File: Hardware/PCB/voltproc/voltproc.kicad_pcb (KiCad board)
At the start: 2 copper layers, 171 x 174 mm, 85 parts, among them J1 Synth_power_2x5, J10 Jack, J11 Jack, J12 Jack, J13 Jack, J14 Jack, J15 Jack, J16 Jack, J17 Jack, J18 Jack, J19 Jack, J2 3_pin_Molex_header, J3 3_pin_Molex_header, J4 Conn_01x13, J7 Conn_01x13, J8 Jack, J9 Jack, SW1 SW_DPDT_x2, SW2 SW_DPDT_x2, U1 TL074, U2 TL074, U3 TL072

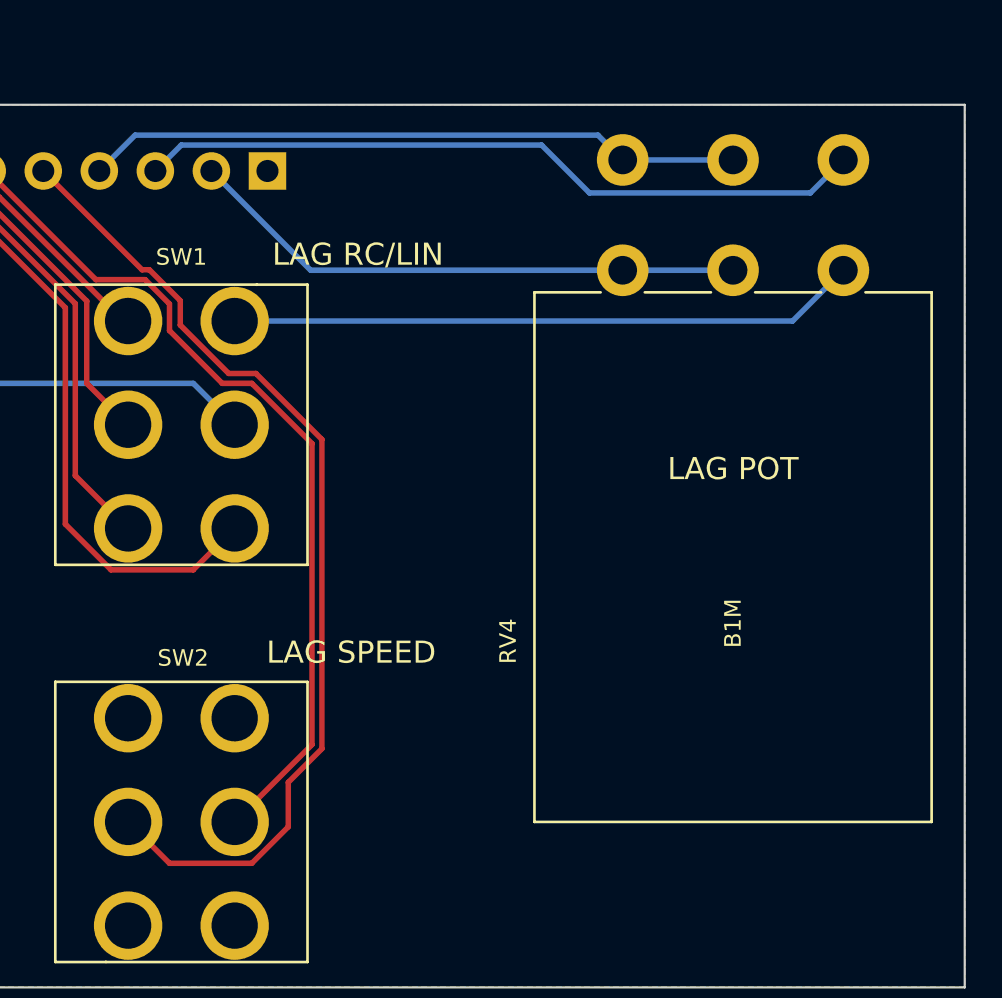
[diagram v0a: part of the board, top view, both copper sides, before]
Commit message: Fix dual pot footprint
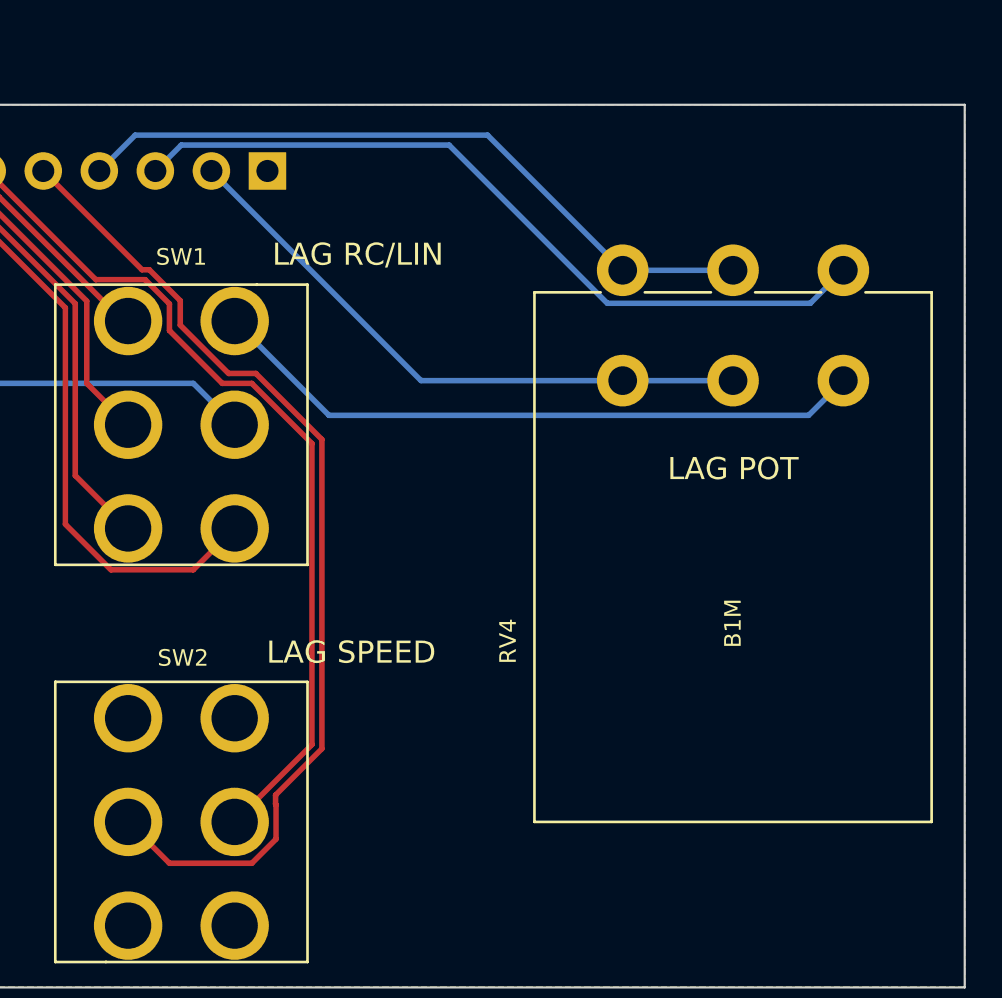
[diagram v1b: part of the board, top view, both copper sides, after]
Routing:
- net /Panel components/LAG_LIN_CCW: track 33.2 -> 35.3 mm
- net /Panel components/LAG_RC_WIP: track 25.5 -> 27.6 mm
- net /Panel components/LAG_LIN_WIP: track 29.9 -> 31.9 mm
- net /Panel components/RC_IN: track 28.5 -> 30.0 mm
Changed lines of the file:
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@@
       (effects (font (size 1 1) (thickness 0.15)))
     )
-    (fp_line (start 9 9) (end -15 9) (layer "F.SilkS") (width 0.12))
+    (fp_line (start -15 4) (end -15 1) (layer "F.SilkS") (width 0.12))
+    (fp_line (start -15 -1) (end -15 -4) (layer "F.SilkS") (width 0.12))
     (fp_line (start -15 -6) (end -15 -9) (layer "F.SilkS") (width 0.12))
+    (fp_line (start 9 9) (end -15 9) (layer "F.SilkS") (width 0.12))
     (fp_line (start -15 9) (end -15 6) (layer "F.SilkS") (width 0.12))
-    (fp_line (start -15 -1) (end -15 -4) (layer "F.SilkS") (width 0.12))
     (fp_line (start -15 -9) (end 9 -9) (layer "F.SilkS") (width 0.12))
-    (fp_line (start -15 4) (end -15 1) (layer "F.SilkS") (width 0.12))
     (fp_line (start 9 -9) (end 9 9) (layer "F.SilkS") (width 0.12))
-    (fp_line (start -22.5 9.5) (end -22.5 -9.5) (layer "F.CrtYd") (width 0.12))
-    (fp_line (start -22.5 -9.5) (end 9.5 -9.5) (layer "F.CrtYd") (width 0.12))
+    (fp_line (start -17.5 9.5) (end -17.5 -9.5) (layer "F.CrtYd") (width 0.12))
     (fp_line (start 9.5 -9.5) (end 9.5 9.5) (layer "F.CrtYd") (width 0.12))
-    (fp_line (start 9.5 9.5) (end -22.5 9.5) (layer "F.CrtYd") (width 0.12))
-    (fp_circle (center 0 0) (end 8.45 0) (layer "F.Fab") (width 0.12) (fill none))
+    (fp_line (start -17.5 -9.5) (end 9.5 -9.5) (layer "F.CrtYd") (width 0.12))
+    (fp_line (start 9.5 9.5) (end -17.5 9.5) (layer "F.CrtYd") (width 0.12))
     (fp_circle (center 0 0) (end 3 0) (layer "F.Fab") (width 0.1) (fill none))
-    (pad "1" thru_hole circle (at -21 -5 270) (size 2.34 2.34) (drill 1.3) (layers *.Cu *.Mask)
+    (fp_circle (center 0 0) (end 8.45 0) (layer "F.Fab") (width 0.12) (fill none))
+    (pad "1" thru_hole circle (at -16 -5 270) (size 2.34 2.34) (drill 1.3) (layers *.Cu *.Mask)
       (net 61 "/Panel components/LAG_LIN_CCW") (pinfunction "1") (pintype "passive"))
-    (pad "2" thru_hole circle (at -21 0 270) (size 2.34 2.34) (drill 1.3) (layers *.Cu *.Mask)
+    (pad "2" thru_hole circle (at -16 0 270) (size 2.34 2.34) (drill 1.3) (layers *.Cu *.Mask)
       (net 62 "/Panel components/LAG_LIN_WIP") (pinfunction "2") (pintype "passive"))
-    (pad "3" thru_hole circle (at -21 5 270) (size 2.34 2.34) (drill 1.3) (layers *.Cu *.Mask)
+    (pad "3" thru_hole circle (at -16 5 270) (size 2.34 2.34) (drill 1.3) (layers *.Cu *.Mask)
       (net 62 "/Panel components/LAG_LIN_WIP") (pinfunction "3") (pintype "passive"))
-    (pad "4" thru_hole circle (at -16 -5 270) (size 2.34 2.34) (drill 1.3) (layers *.Cu *.Mask)
+    (pad "4" thru_hole circle (at -11 -5 270) (size 2.34 2.34) (drill 1.3) (layers *.Cu *.Mask)
       (net 29 "/Panel components/RC_IN") (pinfunction "4") (pintype "passive"))
-    (pad "5" thru_hole circle (at -16 0 270) (size 2.34 2.34) (drill 1.3) (layers *.Cu *.Mask)
+    (pad "5" thru_hole circle (at -11 0 270) (size 2.34 2.34) (drill 1.3) (layers *.Cu *.Mask)
       (net 60 "/Panel components/LAG_RC_WIP") (pinfunction "5") (pintype "passive"))
-    (pad "6" thru_hole circle (at -16 5 270) (size 2.34 2.34) (drill 1.3) (layers *.Cu *.Mask)
+    (pad "6" thru_hole circle (at -11 5 270) (size 2.34 2.34) (drill 1.3) (layers *.Cu *.Mask)
       (net 60 "/Panel components/LAG_RC_WIP") (pinfunction "6") (pintype "passive"))
     (model "${KICAD_AOKICAD}/ao_tht_3d/Potentiometer_Piher_PC-16_Single_Vertical.wrl"
@@
   (segment (start 199.459511 105.733511) (end 201.851489 108.125489) (width 0.25) (layer "F.Cu") (net 23))
   (segment (start 196.125489 103.425489) (end 198.361449 103.425489) (width 0.25) (layer "F.Cu") (net 23))
-  (segment (start 204.843511 126.207193) (end 204.843511 128.222449) (width 0.25) (layer "F.Cu") (net 24))
+  (segment (start 199.949 105.48496) (end 202.140018 107.675978) (width 0.25) (layer "F.Cu") (net 24))
+  (segment (start 204.29 127.223349) (end 204.29 128.776651) (width 0.25) (layer "F.Cu") (net 24))
   (segment (start 206.367511 110.665847) (end 206.367511 124.683193) (width 0.25) (layer "F.Cu") (net 24))
-  (segment (start 203.377643 107.675979) (end 206.367511 110.665847) (width 0.25) (layer "F.Cu") (net 24))
-  (segment (start 202.140018 107.675978) (end 203.377643 107.675979) (width 0.25) (layer "F.Cu") (net 24))
-  (segment (start 193.74 98.5) (end 198.215978 102.975978) (width 0.25) (layer "F.Cu") (net 24))
+  (segment (start 203.19214 129.874511) (end 199.459511 129.874511) (width 0.25) (layer "F.Cu") (net 24))
   (segment (start 199.949 104.377336) (end 199.949 105.48496) (width 0.25) (layer "F.Cu") (net 24))
-  (segment (start 206.367511 124.683193) (end 204.843511 126.207193) (width 0.25) (layer "F.Cu") (net 24))
-  (segment (start 199.949 105.48496) (end 202.140018 107.675978) (width 0.25) (layer "F.Cu") (net 24))
-  (segment (start 203.191449 129.874511) (end 199.459511 129.874511) (width 0.25) (layer "F.Cu") (net 24))
+  (segment (start 204.267 127.200349) (end 204.29 127.223349) (width 0.25) (layer "F.Cu") (net 24))
   (segment (start 198.215978 102.975978) (end 198.547643 102.975979) (width 0.25) (layer "F.Cu") (net 24))
-  (segment (start 198.547643 102.975979) (end 199.949 104.377336) (width 0.25) (layer "F.Cu") (net 24))
-  (segment (start 204.843511 128.222449) (end 203.191449 129.874511) (width 0.25) (layer "F.Cu") (net 24))
   (segment (start 199.459511 129.874511) (end 197.585 128) (width 0.25) (layer "F.Cu") (net 24))
+  (segment (start 204.267 126.783704) (end 204.267 127.200349) (width 0.25) (layer "F.Cu") (net 24))
+  (segment (start 198.547643 102.975979) (end 199.949 104.377336) (width 0.25) (layer "F.Cu") (net 24))
+  (segment (start 206.367511 124.683193) (end 204.267 126.783704) (width 0.25) (layer "F.Cu") (net 24))
+  (segment (start 204.29 128.776651) (end 203.19214 129.874511) (width 0.25) (layer "F.Cu") (net 24))
+  (segment (start 203.377643 107.675979) (end 206.367511 110.665847) (width 0.25) (layer "F.Cu") (net 24))
+  (segment (start 193.74 98.5) (end 198.215978 102.975978) (width 0.25) (layer "F.Cu") (net 24))
+  (segment (start 202.140018 107.675978) (end 203.377643 107.675979) (width 0.25) (layer "F.Cu") (net 24))
   (segment (start 195.710489 108.125489) (end 197.585 110) (width 0.25) (layer "F.Cu") (net 25))
   (segment (start 195.710489 104.396081) (end 195.710489 108.125489) (width 0.25) (layer "F.Cu") (net 25))
@@
   (segment (start 181.04 98.5) (end 190.665489 108.125489) (width 0.25) (layer "B.Cu") (net 28))
   (segment (start 200.540489 108.125489) (end 202.415 110) (width 0.25) (layer "B.Cu") (net 28))
-  (segment (start 227.7 105.3) (end 230 103) (width 0.25) (layer "B.Cu") (net 29))
-  (segment (start 202.415 105.3) (end 227.7 105.3) (width 0.25) (layer "B.Cu") (net 29))
+  (segment (start 202.415 105.3) (end 206.69 109.575) (width 0.25) (layer "B.Cu") (net 29))
+  (segment (start 206.69 109.575) (end 228.425 109.575) (width 0.25) (layer "B.Cu") (net 29))
+  (segment (start 228.425 109.575) (end 230 108) (width 0.25) (layer "B.Cu") (net 29))
   (segment (start 194.742 104.699) (end 194.742 114.50796) (width 0.25) (layer "F.Cu") (net 30))
   (segment (start 184.201 99.873) (end 185.471 101.143) (width 0.25) (layer "F.Cu") (net 30))
@@
   (segment (start 91.12 108.895) (end 91.12 106.355) (width 0.25) (layer "F.Cu") (net 57))
   (segment (start 91.12 106.355) (end 96.185 106.355) (width 0.25) (layer "B.Cu") (net 57))
-  (segment (start 225 103) (end 220 103) (width 0.25) (layer "B.Cu") (net 60))
-  (segment (start 220 103) (end 205.86 103) (width 0.25) (layer "B.Cu") (net 60))
-  (segment (start 205.86 103) (end 201.36 98.5) (width 0.25) (layer "B.Cu") (net 60))
-  (segment (start 216.324489 97.325489) (end 218.493511 99.494511) (width 0.25) (layer "B.Cu") (net 61))
-  (segment (start 199.994511 97.325489) (end 216.324489 97.325489) (width 0.25) (layer "B.Cu") (net 61))
-  (segment (start 228.505489 99.494511) (end 230 98) (width 0.25) (layer "B.Cu") (net 61))
-  (segment (start 198.82 98.5) (end 199.994511 97.325489) (width 0.25) (layer "B.Cu") (net 61))
-  (segment (start 218.493511 99.494511) (end 228.505489 99.494511) (width 0.25) (layer "B.Cu") (net 61))
-  (segment (start 220 98) (end 218.875978 96.875978) (width 0.25) (layer "B.Cu") (net 62))
+  (segment (start 220 108) (end 225 108) (width 0.25) (layer "B.Cu") (net 60))
+  (segment (start 220 108) (end 210.86 108) (width 0.25) (layer "B.Cu") (net 60))
+  (segment (start 210.86 108) (end 201.36 98.5) (width 0.25) (layer "B.Cu") (net 60))
+  (segment (start 199.994521 97.325479) (end 212.133479 97.325479) (width 0.25) (layer "B.Cu") (net 61))
+  (segment (start 219.303 104.495) (end 228.505 104.495) (width 0.25) (layer "B.Cu") (net 61))
+  (segment (start 198.82 98.5) (end 199.994521 97.325479) (width 0.25) (layer "B.Cu") (net 61))
+  (segment (start 212.133479 97.325479) (end 219.303 104.495) (width 0.25) (layer "B.Cu") (net 61))
+  (segment (start 228.505 104.495) (end 230 103) (width 0.25) (layer "B.Cu") (net 61))
   (segment (start 197.904022 96.875978) (end 196.28 98.5) (width 0.25) (layer "B.Cu") (net 62))
-  (segment (start 218.875978 96.875978) (end 197.904022 96.875978) (width 0.25) (layer "B.Cu") (net 62))
-  (segment (start 225 98) (end 220 98) (width 0.25) (layer "B.Cu") (net 62))
+  (segment (start 220 103) (end 225 103) (width 0.25) (layer "B.Cu") (net 62))
+  (segment (start 213.875978 96.875978) (end 197.904022 96.875978) (width 0.25) (layer "B.Cu") (net 62))
+  (segment (start 220 103) (end 213.875978 96.875978) (width 0.25) (layer "B.Cu") (net 62))
   (segment (start 96.272614 168.6) (end 98.578614 166.294) (width 0.25) (layer "B.Cu") (net 63))
   (segment (start 105.064398 166.294) (end 119.418272 151.940126) (width 0.25) (layer "B.Cu") (net 63))

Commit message: final pre fab tweaks
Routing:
- net /Summers/OUT1: track 29.7 -> 28.9 mm
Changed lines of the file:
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@@
   (segment (start 103.81 40.31) (end 116.3916 40.31) (width 0.25) (layer "B.Cu") (net 40))
   (segment (start 116.3916 40.31) (end 120.395 44.3134) (width 0.25) (layer "B.Cu") (net 40))
-  (segment (start 123.704 53.6) (end 124.5 53.6) (width 0.25) (layer "B.Cu") (net 40))
   (segment (start 118.6 85.5) (end 118.6 82.273293) (width 0.25) (layer "F.Cu") (net 41))
   (segment (start 128.813293 72.06) (end 130.48 72.06) (width 0.25) (layer "F.Cu") (net 41))

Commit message: R7->47k; documentation and photos
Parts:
- R7: value 4.7k -> 47k

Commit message: Glare at one nonconformist jack and make it behave
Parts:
- turned J17 to -90 degrees
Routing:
- net /Summers/~{OUT1}: track 19.3 -> 9.02 mm
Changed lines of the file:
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@@
   )
   (footprint "ao_tht:Jack_6.35mm_PJ_629HAN_slots" (layer "F.Cu")
-    (at 125 85)
+    (at 125 85 -90)
     (property "Description" "1/4\" audio jack")
     (property "Sheetfile" "voltproc_summers.kicad_sch")
     (property "Sheetname" "Summers")
     (attr through_hole)
-    (fp_text reference "J17" (at 0 -9.5) (layer "F.SilkS")
+    (fp_text reference "J17" (at 0 -9.5 90) (layer "F.SilkS")
       (effects (font (size 0.75 0.75) (thickness 0.15)))
     )
-    (fp_text value "Jack" (at 0 10) (layer "F.Fab")
+    (fp_text value "Jack" (at 0 10 90) (layer "F.Fab")
       (effects (font (size 1 1) (thickness 0.15)))
     )
@@
     (fp_line (start -7.994 -7.99) (end 7.954 -7.99) (layer "F.Fab") (width 0.12))
     (fp_line (start 5.414 7.958) (end -7.994 7.958) (layer "F.Fab") (width 0.12))
-    (pad "R" thru_hole oval (at 0.5 -6.4) (size 4.500001 2.5) (drill oval 2.7 1) (layers *.Cu *.Mask))
-    (pad "RN" thru_hole oval (at 6.4 -2.5) (size 2.500001 4.500001) (drill oval 1 2.7) (layers *.Cu *.Mask))
-    (pad "S" thru_hole rect (at 4.74 4.74 45) (size 4.500001 2.500001) (drill oval 2.7 1) (layers *.Cu *.Mask)
+    (pad "R" thru_hole oval (at 0.5 -6.4 270) (size 4.500001 2.5) (drill oval 2.7 1) (layers *.Cu *.Mask))
+    (pad "RN" thru_hole oval (at 6.4 -2.5 270) (size 2.500001 4.500001) (drill oval 1 2.7) (layers *.Cu *.Mask))
+    (pad "S" thru_hole rect (at 4.74 4.74 315) (size 4.500001 2.500001) (drill oval 2.7 1) (layers *.Cu *.Mask)
       (net 2 "GND") (pintype "passive"))
-    (pad "T" thru_hole oval (at -6.4 0.5) (size 2.5 4.5) (drill oval 1 2.7) (layers *.Cu *.Mask)
+    (pad "T" thru_hole oval (at -6.4 0.5 270) (size 2.5 4.5) (drill oval 1 2.7) (layers *.Cu *.Mask)
       (net 41 "/Summers/~{OUT1}") (pintype "passive"))
-    (pad "TN" thru_hole oval (at -2.5 6.4) (size 4.5 2.5) (drill oval 2.7 1) (layers *.Cu *.Mask))
+    (pad "TN" thru_hole oval (at -2.5 6.4 270) (size 4.5 2.5) (drill oval 2.7 1) (layers *.Cu *.Mask))
     (model "${KICAD_AOKICAD}/ao_tht_3d/User Library-jack-4.STEP"
       (offset (xyz 0 0 23))
@@
   (segment (start 103.81 40.31) (end 116.3916 40.31) (width 0.25) (layer "B.Cu") (net 40))
   (segment (start 116.3916 40.31) (end 120.395 44.3134) (width 0.25) (layer "B.Cu") (net 40))
-  (segment (start 118.6 85.5) (end 118.6 82.273293) (width 0.25) (layer "F.Cu") (net 41))
-  (segment (start 128.813293 72.06) (end 130.48 72.06) (width 0.25) (layer "F.Cu") (net 41))
-  (segment (start 118.6 82.273293) (end 128.813293 72.06) (width 0.25) (layer "F.Cu") (net 41))
+  (segment (start 124.5 78.04) (end 124.5 78.6) (width 0.25) (layer "F.Cu") (net 41))
+  (segment (start 130.48 72.06) (end 124.5 78.04) (width 0.25) (layer "F.Cu") (net 41))
   (segment (start 115.365 130.48) (end 121.59 130.48) (width 0.25) (layer "B.Cu") (net 42))
   (segment (start 101.866 143.6) (end 110.046 135.42) (width 0.25) (layer "B.Cu") (net 42))
